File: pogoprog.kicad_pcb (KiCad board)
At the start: 2 copper layers, 50 x 21.8 mm, 12 parts, among them J3 Conn_02x06_Odd_Even, M1 Arduino_Mini

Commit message: Moved some silkscreen text.
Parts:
- moved PRG 0.63 mm to (147.3, 99.8)
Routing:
- net Net-(JP4-B): track 2.79 -> 3.81 mm
- net +5V: track 41.0 -> 41.6 mm
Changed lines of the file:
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@@
   )
   (footprint "Jumper:SolderJumper-2_P1.3mm_Open_Pad1.0x1.5mm" (layer "B.Cu")
-    (at 146.7 99.75)
+    (at 147.33 99.78)
     (descr "SMD Solder Jumper, 1x1.5mm Pads, 0.3mm gap, open")
     (tags "solder jumper open")
@@
     (property "ki_keywords" "Jumper SPST")
     (attr exclude_from_pos_files)
-    (fp_text reference "PRG" (at -2.3 -0.1 -90) (layer "B.SilkS")
+    (fp_text reference "PRG" (at -3.02 -0.11) (layer "B.SilkS")
         (effects (font (size 1 1) (thickness 0.15)) (justify mirror))
     )
@@
   (gr_line (start 149.6 100) (end 149.6 80.6)
     (stroke (width 0.1) (type solid)) (layer "Edge.Cuts"))
-  (gr_text "JLCJLCJLCJLC" (at 143.9 91.05 90) (layer "B.SilkS")
-    (effects (font (size 0.8 0.8) (thickness 0.12)) (justify mirror))
-  )
   (gr_text "mjd 23-May-23" (at 142.15 80.65) (layer "B.SilkS")
     (effects (font (size 1 1) (thickness 0.15)) (justify mirror))
@@
   (gr_text "v1.4a" (at 146.25 80.55) (layer "F.SilkS")
     (effects (font (size 1 1) (thickness 0.15)))
+  )
+  (gr_text "JLCJLCJLCJLC" (at 142.64 91.1 90) (layer "F.SilkS")
+    (effects (font (size 0.8 0.8) (thickness 0.12)))
   )
   (gr_text "PRG" (at 124.72 80.6) (layer "F.SilkS")
@@
   (segment (start 141.1 85.35) (end 141.1 96.05) (width 0.5) (layer "F.Cu") (net 6))
   (via (at 141.1 96.05) (size 0.7) (drill 0.3) (layers "F.Cu" "B.Cu") (net 6))
+  (segment (start 146.01 100.45) (end 146.68 99.78) (width 0.5) (layer "B.Cu") (net 6))
+  (segment (start 133.45 100.45) (end 146.01 100.45) (width 0.5) (layer "B.Cu") (net 6))
   (segment (start 131.72 98.72) (end 133.45 100.45) (width 0.5) (layer "B.Cu") (net 6))
-  (segment (start 133.45 100.45) (end 145.35 100.45) (width 0.5) (layer "B.Cu") (net 6))
   (segment (start 134.39 96.05) (end 141.1 96.05) (width 0.5) (layer "B.Cu") (net 6))
   (segment (start 131.72 98.72) (end 134.39 96.05) (width 0.5) (layer "B.Cu") (net 6))
-  (segment (start 145.35 100.45) (end 146.05 99.75) (width 0.5) (layer "B.Cu") (net 6))
   (segment (start 103.78 98.72) (end 108.9 93.6) (width 0.5) (layer "B.Cu") (net 7))
   (segment (start 144.746522 93.6) (end 144.756522 93.59) (width 0.5) (layer "B.Cu") (net 7))
@@
   (segment (start 108.9 93.6) (end 144.746522 93.6) (width 0.5) (layer "B.Cu") (net 7))
   (segment (start 147.865 92.32) (end 146.595 93.59) (width 0.37) (layer "B.Cu") (net 7))
-  (segment (start 147.4875 100.05) (end 148.75 100.05) (width 0.5) (layer "F.Cu") (net 8))
-  (via (at 148.75 100.05) (size 0.7) (drill 0.3) (layers "F.Cu" "B.Cu") (net 8))
-  (segment (start 147.65 100.05) (end 147.35 99.75) (width 0.5) (layer "B.Cu") (net 8))
-  (segment (start 148.75 100.05) (end 147.65 100.05) (width 0.5) (layer "B.Cu") (net 8))
+  (segment (start 147.62 100.05) (end 149.07 98.6) (width 0.5) (layer "F.Cu") (net 8))
+  (segment (start 147.4875 100.05) (end 147.62 100.05) (width 0.5) (layer "F.Cu") (net 8))
+  (via (at 149.07 98.6) (size 0.7) (drill 0.3) (layers "F.Cu" "B.Cu") (net 8))
+  (segment (start 147.98 99.78) (end 147.98 99.69) (width 0.5) (layer "B.Cu") (net 8))
+  (segment (start 147.98 99.69) (end 149.07 98.6) (width 0.5) (layer "B.Cu") (net 8))
   (segment (start 142.2 96.05) (end 142.1 95.95) (width 0.5) (layer "F.Cu") (net 9))
   (segment (start 142.1 95.95) (end 142.1 87.75) (width 0.5) (layer "F.Cu") (net 9))

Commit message: Added pads for a common-anode 8mm RGB LED
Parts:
- added D4: LED_RAGB, aalib:LED_D8.0mm-4_RGB, F.Cu at (139.2, 80.6)
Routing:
- net Net-(D1-A): track 1.90 -> 41.5 mm, vias 0 -> 1
- net Net-(D3-A): track 1.90 -> 32.5 mm, vias 0 -> 1
- net Net-(D2-A): track 1.90 -> 10.7 mm, vias 0 -> 1
- net /D7: track 10.5 -> 2.88 mm
- net +5V: track 41.6 -> 46.4 mm
- net /D8: track 15.2 -> 18.6 mm, vias 0 -> 1
- net GND: track 57.9 -> 59.3 mm
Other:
- board text added: "mjd 14-Aug-23"
- board text added: "v1.5a"
- board text removed: "mjd 23-May-23"
- board text removed: "v1.4a"

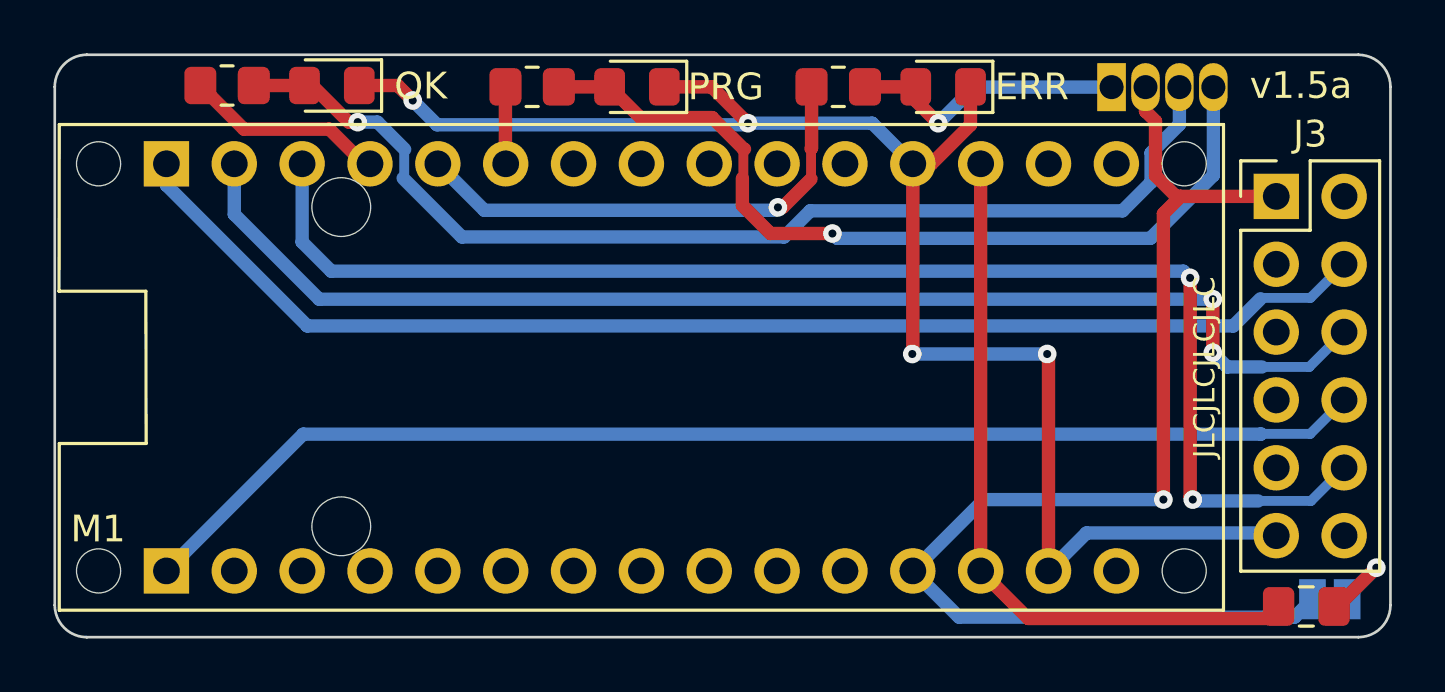
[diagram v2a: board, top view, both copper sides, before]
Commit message: Last minute tweaks
Improved silkscreen for LED labels.
Added text to back showing connector pinout
Moved M1
Renamed J3 to J1
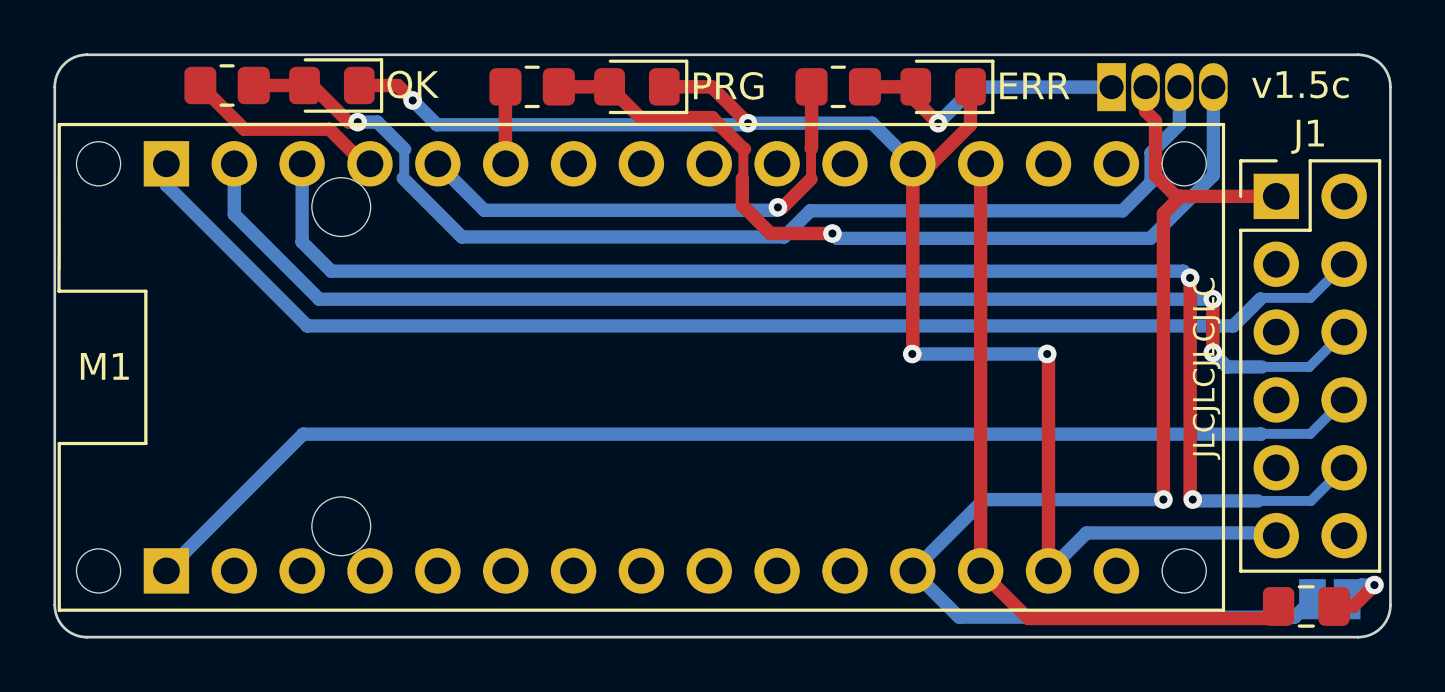
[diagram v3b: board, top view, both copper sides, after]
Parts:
- renumbered J3 to J1, PRG to PRG1
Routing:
- net Net-(PRG1-B): track 3.81 -> 3.08 mm
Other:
- board text added: "mjd 15-Sep-23"
- board text added: "v1.5c"
- board text added: "• 5V MISO • MOSI • SCK • SS • • GND"
- board text removed: "mjd 14-Aug-23"
- board text removed: "v1.5a"
